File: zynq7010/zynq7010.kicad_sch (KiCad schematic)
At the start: 131 parts, among them J1 Conn_02x15_Odd_Even, U1 xc7z010clg400, U2 TPS563200, U3 TPS563200, U4 TPS563200, U5 TPS563200, U6 MT41K256M16HA, U7 MT41K256M16HA

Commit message: finish dcdc and vtt sch, later do crystal and sd card
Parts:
- removed C28, C29: 100nF, Capacitor_SMD:C_0402_1005Metric, symbol Device:C
- removed C30: 10uF, Capacitor_SMD:C_0402_1005Metric, symbol Device:C
- removed R15: 1k, Resistor_SMD:R_0402_1005Metric, symbol Device:R
- removed R9: 13.7k, Resistor_SMD:R_0402_1005Metric, symbol Device:R
- added C35: 4.7uF, Capacitor_SMD:C_0402_1005Metric, symbol Device:C
- added C37, C38, C39, C40, C41, C48, C51, C52: 10uF, Capacitor_SMD:C_0402_1005Metric, symbol Device:C
- added C42, C43: 47uF, Capacitor_SMD:C_0402_1005Metric, symbol Device:C
- added C44, C46: 100nF, Capacitor_SMD:C_0402_1005Metric, symbol Device:C
- added C45, C47, C49, C50: 0.1uF, Capacitor_SMD:C_0402_1005Metric, symbol Device:C
- added R14, R18, R19, R25, R26, R27: 10k, Resistor_SMD:R_0402_1005Metric, symbol Device:R
- added R17: 3.3k, Resistor_SMD:R_0402_1005Metric, symbol Device:R
- added R20: 3k, Resistor_SMD:R_0402_1005Metric, symbol Device:R
- added U6: TPS51200DRC, Package_SON:VSON-10-1EP_3x3mm_P0.5mm_EP1.65x2.4mm, symbol Regulator_Linear:TPS51200DRC
- R11: value 13.7k -> 7.5k
- R12: renamed from R5; value 13.7k -> 3k
- R15: renamed from R7; value 13.7k -> 10k
- R16: value 1k -> 2k
- renumbered C46 to C13, C13 to C14, C14 to C15, C15 to C16, C45 to C17, C16 to C18, C17 to C19, C18 to C20, C19 to C21, C20 to C22, C21 to C23, C22 to C25, C25 to C26, C26 to C27, C23 to C28, C47 to C29, C27 to C30, C52 to C31, C48 to C32, C51 to C33, C49 to C34, C50 to C36, C63 to C54, C54 to C55, C64 to C56, C55 to C57, C65 to C58, C56 to C59, C66 to C60, C57 to C61, C67 to C62, C58 to C63, C68 to C64, C69 to C65, C59 to C66, C60 to C67, C70 to C68, C37 to C69, C71 to C70, C61 to C71, C32 to C72, C62 to C73, C72 to C74, C33 to C75, C31 to C76, C73 to C77, C34 to C78, C74 to C79, C35 to C80, C36 to C81, C38 to C82, R22 to R1, R8 to R10, R6 to R13, R1 to R2, R51 to R21, R52 to R22, R24 to R23, R53 to R24, R18 to R28, R26 to R29, R2 to R3, R27 to R30, R28 to R31, R29 to R32, R30 to R33, R31 to R34, R32 to R35, R33 to R36, R34 to R37, R35 to R38, R36 to R39, R3 to R4, R37 to R40, R38 to R41, R39 to R42, R40 to R43, R19 to R44, R41 to R45, R42 to R46, R43 to R47, R44 to R48, R45 to R49, R4 to R5, R46 to R50, R47 to R51, R48 to R52, R49 to R53, R50 to R54, R20 to R55, R17 to R56, R25 to R57, R23 to R6, R21 to R7, R12 to R8, R10 to R9, U2 to U1, U3 to U2, U4 to U3, U5 to U4, U1 to U5, U6 to U8
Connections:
- net +1V5: now also R16.2, C37.2, C38.2, R26.1, U6.2 (VLDOIN)
- net +1V8: now also R17.2; no longer R15.1
- net +3V3: now also C35.1, C42.2, C43.2, C45.2, C47.2, C49.2, C50.2, C51.2, C52.2, R20.2, R25.2, U6.10 (VIN), U6.7 (EN); no longer R11.1
- net GND: now also C35.2, C37.1, C38.1, C39.2, C40.2, C41.2, C42.1, C43.1, C44.2, C45.1, C46.2, C47.1, C48.2, C49.1, C50.1, C51.1, C52.1, R27.2, U6.11 (GND), U6.4 (GND), U6.8 (GND); no longer R16.1
- net VREF_DDR: now also C44.1, C48.1, U6.6 (REFOUT); no longer R16.2
- net VTT_DDR3: now also C39.1, C40.1, C41.1, U6.3 (VO), U6.5 (VOSNS)
- net at R8.1, U4.4 (VFB): now also R14.1; no longer R11.2
- net at R10.1, U2.4 (VFB): now also R15.1; no longer R15.2
- net at R9.1, U3.4 (VFB): now also R11.1
- new net: R14.2, R18.1
- new net: R18.2, R19.1
- new net: R19.2, R20.1
- new net: R11.2, R16.1
- new net: C46.1, R26.2, R27.1, U6.1 (REFIN)
- new net: R25.1, U6.9 (PGOOD)
- new net: R15.2, R17.1
- no-connect marks 65 -> 165
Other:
- note removed: "later draw voltage regulator for ddr3 termination"
- moved on the sheet: C22, C23, C24, C25, C26, C27, C28, C29, C30, C31, C32, C33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

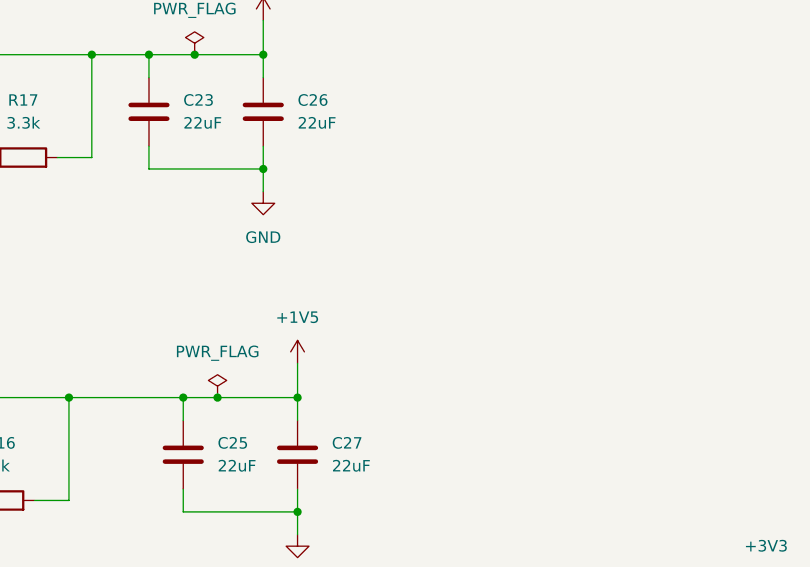
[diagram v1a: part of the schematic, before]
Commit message: done routing between two ddr3
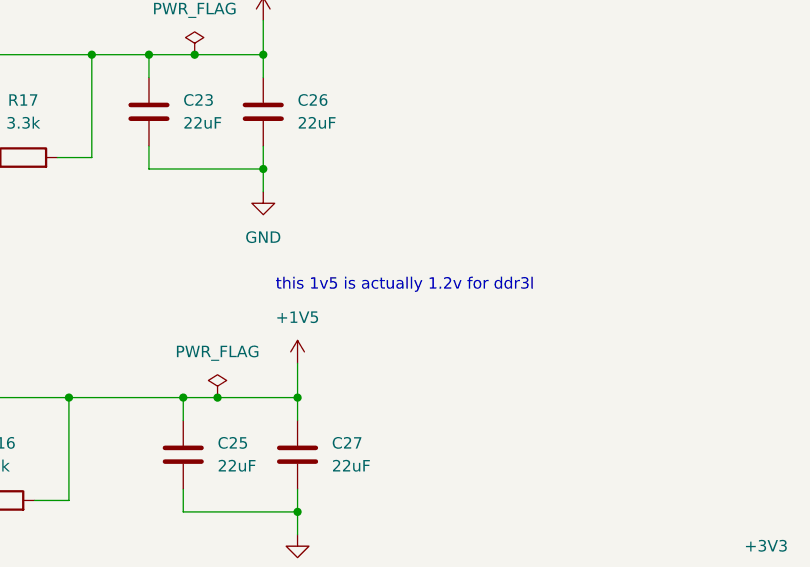
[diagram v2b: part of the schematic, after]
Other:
- note added: "this 1v5 is actually 1.2v for ddr3l"
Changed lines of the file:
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@@
+		)
+	)
+	(text "this 1v5 is actually 1.2v for ddr3l"
+		(exclude_from_sim no)
+		(at 157.988 317.754 0)
+		(effects
+			(font
+				(size 1.27 1.27)
+			)
 		)
 	)

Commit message: done routing between zynq and two ddr3, not gonna do length matching
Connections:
- net DQ0: now also U7.H7 (DQ7); no longer U7.F8 (DQ3)
- net DQ13: now also U7.A3 (DQ15); no longer U7.C2 (DQ11)
- net DQ17: now also U8.H7 (DQ7); no longer U8.G2 (DQ6)
- net DQ18: now also U8.H3 (DQ4); no longer U8.E3 (DQ0)
- net DQ19: now also U8.E3 (DQ0); no longer U8.H3 (DQ4)
- net DQ2: now also U7.G2 (DQ6); no longer U7.F2 (DQ2)
- net DQ21: now also U8.F8 (DQ3); no longer U8.H8 (DQ5)
- net DQ22: now also U8.H8 (DQ5); no longer U8.H7 (DQ7)
- net DQ23: now also U8.G2 (DQ6); no longer U8.F8 (DQ3)
- net DQ4: now also U7.H8 (DQ5); no longer U7.F7 (DQ1)
- net DQ5: now also U7.F8 (DQ3); no longer U7.H7 (DQ7)
- net DQ6: now also U7.F2 (DQ2); no longer U7.G2 (DQ6)
- net DQ7: now also U7.F7 (DQ1); no longer U7.H8 (DQ5)
- net DQ8: now also U7.C3 (DQ9); no longer U7.A3 (DQ15)
- net DQ9: now also U7.C2 (DQ11); no longer U7.C3 (DQ9)
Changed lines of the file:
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@@
+		)
+	)
+	(label "DQ5"
+		(at 556.26 40.64 0)
+		(effects
+			(font
+				(size 1.27 1.27)
+			)
+			(justify left bottom)
 		)
 	)
@@
 		)
 	)
-	(label "DQ6"
-		(at 556.26 48.26 0)
-		(effects
-			(font
-				(size 1.27 1.27)
-			)
-			(justify left bottom)
-		)
-	)
 	(label "BA1"
 		(at 468.63 266.7 0)
@@
 		)
 	)
+	(label "DQ18"
+		(at 556.26 158.75 0)
+		(effects
+			(font
+				(size 1.27 1.27)
+			)
+			(justify left bottom)
+		)
+	)
 	(label "DQ14"
 		(at 556.26 63.5 0)
@@
 		)
 	)
-	(label "DQ8"
-		(at 556.26 71.12 0)
-		(effects
-			(font
-				(size 1.27 1.27)
-			)
-			(justify left bottom)
-		)
-	)
 	(label "LDQS1"
 		(at 439.42 191.77 180)
@@
 		)
 	)
+	(label "DQ9"
+		(at 556.26 60.96 0)
+		(effects
+			(font
+				(size 1.27 1.27)
+			)
+			(justify left bottom)
+		)
+	)
 	(label "A11"
 		(at 439.42 54.61 180)
@@
 		)
 	)
+	(label "DQ8"
+		(at 556.26 55.88 0)
+		(effects
+			(font
+				(size 1.27 1.27)
+			)
+			(justify left bottom)
+		)
+	)
 	(label "TDI_0"
 		(at 67.31 77.47 180)
@@
 		)
 	)
+	(label "DQ7"
+		(at 556.26 35.56 0)
+		(effects
+			(font
+				(size 1.27 1.27)
+			)
+			(justify left bottom)
+		)
+	)
 	(label "A1"
 		(at 505.46 35.56 180)
@@
 		)
 	)
+	(label "DQ22"
+		(at 556.26 161.29 0)
+		(effects
+			(font
+				(size 1.27 1.27)
+			)
+			(justify left bottom)
+		)
+	)
 	(label "DQ5"
 		(at 439.42 107.95 180)
@@
 		)
 	)
-	(label "DQ23"
-		(at 556.26 156.21 0)
-		(effects
-			(font
-				(size 1.27 1.27)
-			)
-			(justify left bottom)
-		)
-	)
 	(label "~{CK}"
 		(at 505.46 274.32 180)
@@
 		)
 	)
-	(label "DQ17"
-		(at 556.26 163.83 0)
-		(effects
-			(font
-				(size 1.27 1.27)
-			)
-			(justify left bottom)
-		)
-	)
 	(label "~{CK}"
 		(at 505.46 227.33 180)
@@
 		)
 	)
-	(label "DQ0"
-		(at 556.26 40.64 0)
-		(effects
-			(font
-				(size 1.27 1.27)
-			)
-			(justify left bottom)
-		)
-	)
 	(label "DQ24"
 		(at 556.26 171.45 0)
@@
 		)
 	)
-	(label "DQ9"
-		(at 556.26 55.88 0)
-		(effects
-			(font
-				(size 1.27 1.27)
-			)
-			(justify left bottom)
-		)
-	)
 	(label "A8"
 		(at 505.46 168.91 180)
@@
 		)
 	)
-	(label "DQ21"
-		(at 556.26 161.29 0)
-		(effects
-			(font
-				(size 1.27 1.27)
-			)
-			(justify left bottom)
-		)
-	)
 	(label "BA0"
 		(at 439.42 64.77 180)
@@
 		)
 	)
+	(label "DQ4"
+		(at 556.26 45.72 0)
+		(effects
+			(font
+				(size 1.27 1.27)
+			)
+			(justify left bottom)
+		)
+	)
 	(label "DQ19"
 		(at 439.42 143.51 180)
@@
 		)
 	)
-	(label "DQ2"
-		(at 556.26 38.1 0)
-		(effects
-			(font
-				(size 1.27 1.27)
-			)
-			(justify left bottom)
-		)
-	)
 	(label "~{WE}"
 		(at 505.46 93.98 180)
@@
 		)
 	)
+	(label "DQ2"
+		(at 556.26 48.26 0)
+		(effects
+			(font
+				(size 1.27 1.27)
+			)
+			(justify left bottom)
+		)
+	)
 	(label "~{UDQS}0"
 		(at 439.42 179.07 180)
@@
 		)
 	)
+	(label "DQ0"
+		(at 556.26 50.8 0)
+		(effects
+			(font
+				(size 1.27 1.27)
+			)
+			(justify left bottom)
+		)
+	)
 	(label "A14"
 		(at 505.46 68.58 180)
@@
 		)
 	)
-	(label "DQ4"
-		(at 556.26 35.56 0)
-		(effects
-			(font
-				(size 1.27 1.27)
-			)
-			(justify left bottom)
-		)
-	)
 	(label "PS_SRST_B_501"
 		(at 93.98 176.53 0)
@@
 		)
 	)
+	(label "DQ6"
+		(at 556.26 38.1 0)
+		(effects
+			(font
+				(size 1.27 1.27)
+			)
+			(justify left bottom)
+		)
+	)
+	(label "DQ17"
+		(at 556.26 166.37 0)
+		(effects
+			(font
+				(size 1.27 1.27)
+			)
+			(justify left bottom)
+		)
+	)
+	(label "DQ19"
+		(at 556.26 148.59 0)
+		(effects
+			(font
+				(size 1.27 1.27)
+			)
+			(justify left bottom)
+		)
+	)
 	(label "DQ18"
 		(at 439.42 140.97 180)
@@
 		)
 	)
-	(label "DQ13"
-		(at 556.26 60.96 0)
-		(effects
-			(font
-				(size 1.27 1.27)
-			)
-			(justify left bottom)
-		)
-	)
 	(label "~{LDQS}1"
 		(at 556.26 196.85 0)
@@
 		)
 	)
+	(label "DQ23"
+		(at 556.26 163.83 0)
+		(effects
+			(font
+				(size 1.27 1.27)
+			)
+			(justify left bottom)
+		)
+	)
 	(label "A10"
 		(at 505.46 58.42 180)
@@
 		)
 	)
-	(label "DQ18"
-		(at 556.26 148.59 0)
-		(effects
-			(font
-				(size 1.27 1.27)
-			)
-			(justify left bottom)
-		)
-	)
 	(label "DQ24"
 		(at 439.42 156.21 180)
@@
 		)
 	)
-	(label "DQ5"
-		(at 556.26 50.8 0)
-		(effects
-			(font
-				(size 1.27 1.27)
-			)
-			(justify left bottom)
-		)
-	)
 	(label "A11"
 		(at 505.46 60.96 180)
@@
 		)
 	)
-	(label "DQ19"
-		(at 556.26 158.75 0)
-		(effects
-			(font
-				(size 1.27 1.27)
-			)
-			(justify left bottom)
-		)
-	)
 	(label "DQ0"
 		(at 439.42 95.25 180)
@@
 		)
 	)
-	(label "DQ22"
-		(at 556.26 166.37 0)
-		(effects
-			(font
-				(size 1.27 1.27)
-			)
-			(justify left bottom)
-		)
-	)
 	(label "A9"
 		(at 439.42 49.53 180)
@@
 		)
 	)
+	(label "DQ13"
+		(at 556.26 71.12 0)
+		(effects
+			(font
+				(size 1.27 1.27)
+			)
+			(justify left bottom)
+		)
+	)
 	(label "UDQS1"
 		(at 556.26 201.93 0)
@@
 		)
 	)
+	(label "DQ21"
+		(at 556.26 156.21 0)
+		(effects
+			(font
+				(size 1.27 1.27)
+			)
+			(justify left bottom)
+		)
+	)
 	(label "A4"
 		(at 505.46 43.18 180)
@@
 		)
 	)
-	(label "DQ7"
-		(at 556.26 45.72 0)
-		(effects
-			(font
-				(size 1.27 1.27)
-			)
-			(justify left bottom)
-		)
-	)
